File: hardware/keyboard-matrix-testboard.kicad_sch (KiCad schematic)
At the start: 86 parts, among them J2 TC2030-IDC-NL, J2 USB_B_Micro, J3 EZmate-4, J6 EZmate-3, Q1 BSS84, SW1 SW_Push, U1 nRF52832-QFxx, U2 PCAL6408A, U3 STBC08, U8 MIC5301, Y1 32.768kHz, Y2 32MHz

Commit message: hw: schematic tweaks
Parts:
- D21, D23, D8, SW1: now fitted
- R1: value 1k -> 4k7
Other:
- moved on the sheet: AE1, C12, C13, C14, C3, C30, C32, C8, D10, D11, D12, D13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

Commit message: hw: assembly tweaks
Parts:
- D2: value Green -> Yellow
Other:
- note added: "<- should have been batt"
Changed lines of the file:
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@@
     (effects (font (size 1.27 1.27)) (justify right bottom))
+  )
+  (text "<- should have been batt" (at 175.26 20.32 0)
+    (effects (font (size 1.27 1.27)) (justify left bottom))
   )
   (text "UARTs" (at 154.94 151.13 0)
@@
   (symbol (lib_id "Device:LED") (at 142.24 33.02 90) (unit 1)
     (in_bom yes) (on_board yes) (dnp no) (fields_autoplaced)
-    (property "Reference" "D2" (at 146.05 33.3374 90)
+    (property "Reference" "D2" (at 146.05 33.3375 90)
       (effects (font (size 1.27 1.27)) (justify right))
     )
-    (property "Value" "Green" (at 146.05 35.8774 90)
+    (property "Value" "Yellow" (at 146.05 35.8775 90)
       (effects (font (size 1.27 1.27)) (justify right))
     )

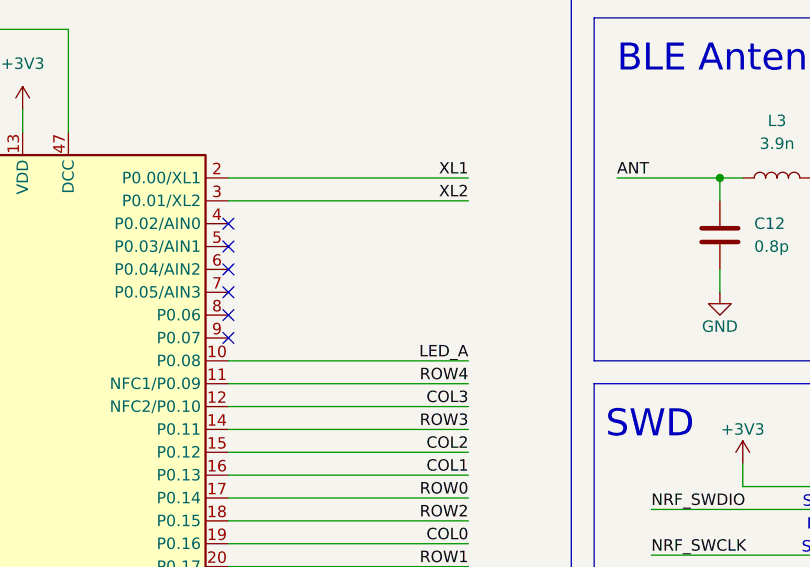
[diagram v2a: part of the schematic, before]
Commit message: hw: add a note about the missing adc_vbatt connection
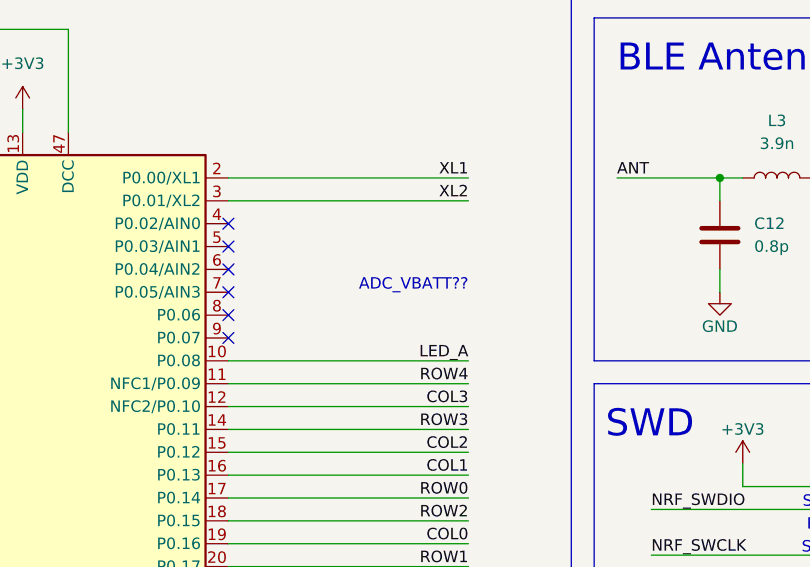
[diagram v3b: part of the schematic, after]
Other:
- note added: "ADC_VBATT??"
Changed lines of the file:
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@@
     (effects (font (size 1.27 1.27)) (justify left bottom))
+  )
+  (text "ADC_VBATT??" (at 139.7 99.06 0)
+    (effects (font (size 1.27 1.27)) (justify right bottom))
   )
   (text "VCC" (at 182.88 120.65 0)
